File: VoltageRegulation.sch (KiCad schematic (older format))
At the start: 83 parts, among them Q201 TIP41, Q202 TIP41, Q203 TIP42, U201 LM7812_TO220, U202 LM7805_TO220, U203 Step Down Module +15 to 7v - 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, U204 LM7912_TO220, U205 XL6009 Module DCDC 19 to 30v, U206 TL071, U207 LM78M05_TO252, U208 LM78M12_TO252, U209 MC79M12_TO252

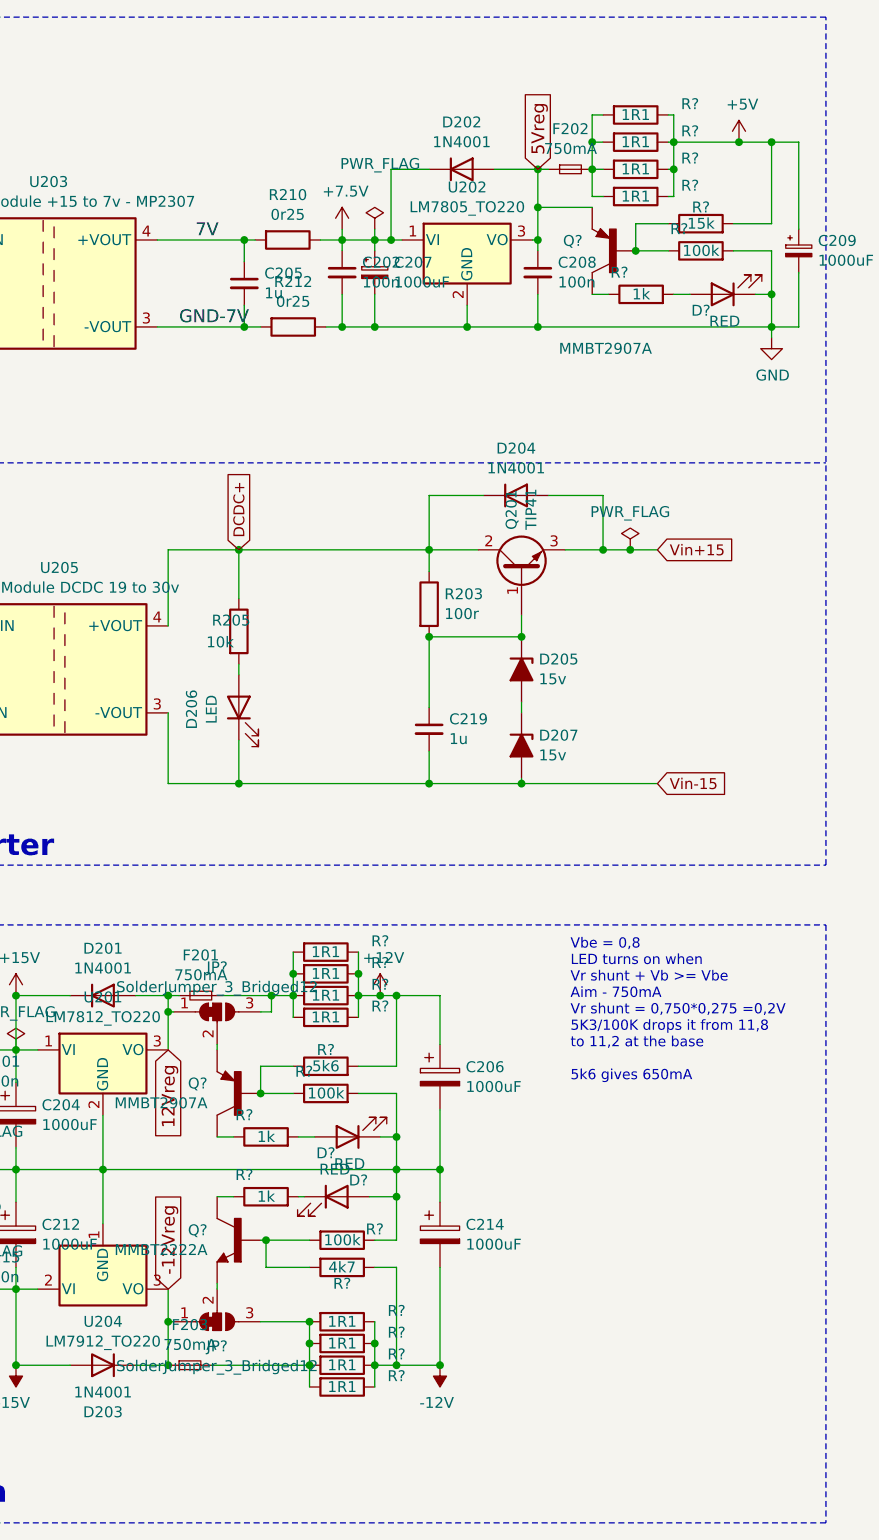
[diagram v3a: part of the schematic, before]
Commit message: placing first components
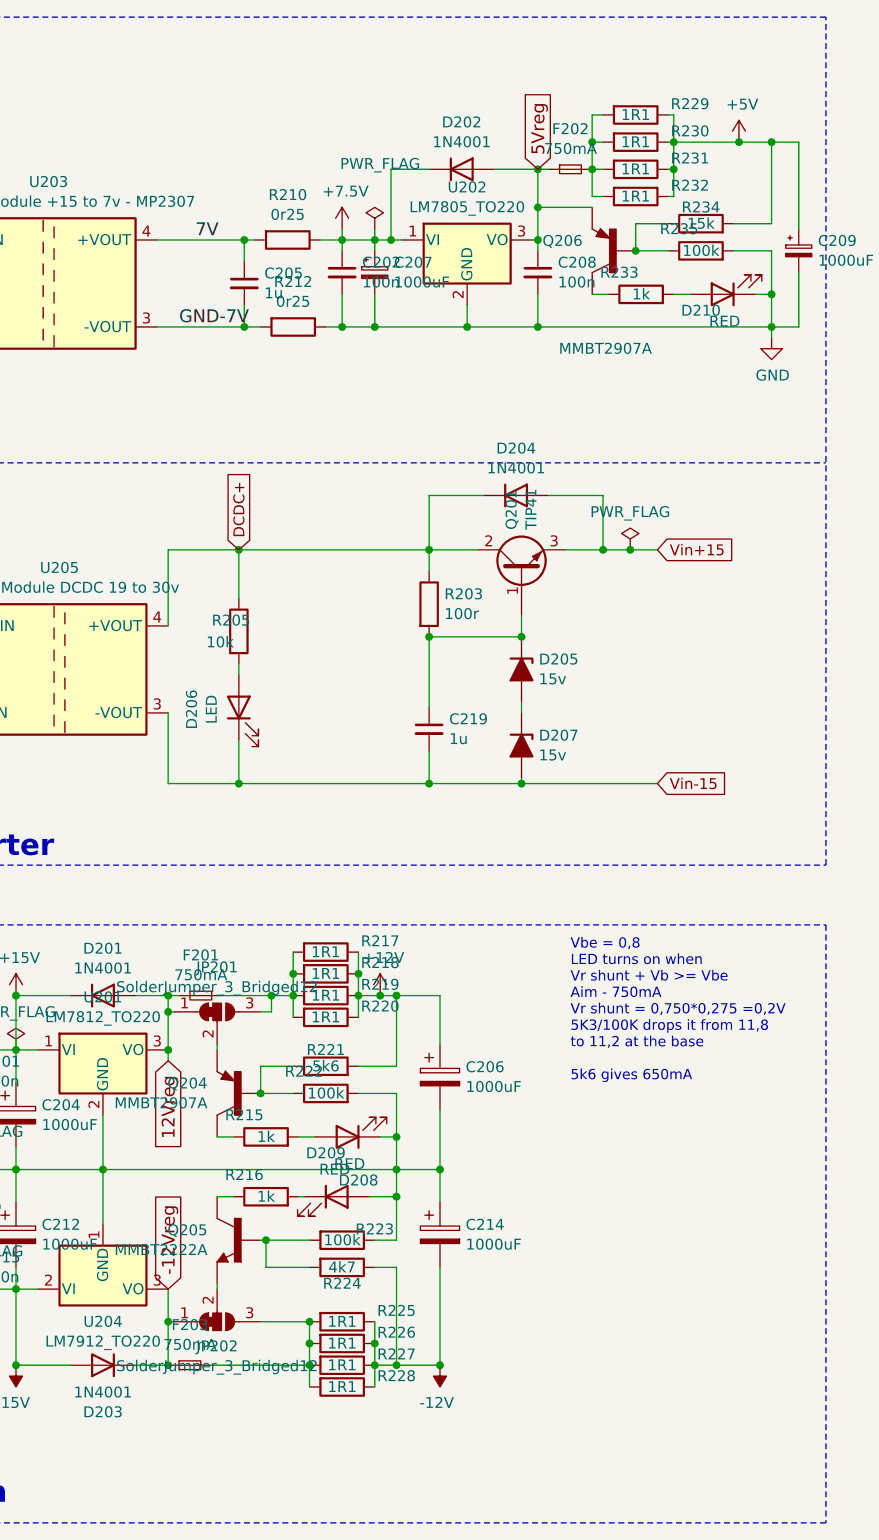
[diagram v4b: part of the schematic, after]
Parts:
- gave numbers to parts that had none: 29
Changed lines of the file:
@@
 Text GLabel 2675 6525 1    59   Input ~ 0
 -12Vreg
-Text GLabel 2675 5425 3    59   Input ~ 0
+Text GLabel 2675 5475 3    59   Input ~ 0
 12Vreg
 $Comp
@@
 U 1 1 5E8B7031
 P 3000 5625
-F 0 "Q?" H 3144 5671 50  0000 L CNN
+AR Path="/5E8B7031" Ref="Q?"  Part="1"
+AR Path="/5CBAA806/5E8B7031" Ref="Q204"  Part="1"
+F 0 "Q204" H 3144 5671 50  0000 L CNN
 F 1 "MMBT2907A" H 3144 5580 50  0000 L CNN
 F 2 "" H 3000 5625 98  0001 C CNN
@@
 U 1 1 5E8B7037
 P 3650 5175
-F 0 "#PWR?" H 3650 5025 50  0001 C CNN
+AR Path="/5E8B7037" Ref="#PWR?"  Part="1"
+AR Path="/5CBAA806/5E8B7037" Ref="#PWR0208"  Part="1"
+F 0 "#PWR0208" H 3650 5025 50  0001 C CNN
 F 1 "+12V" H 3665 5348 50  0000 C CNN
 F 2 "" H 3650 5175 50  0001 C CNN
@@
 U 1 1 5E8B7043
 P 3400 5175
-F 0 "R?" V 3350 5425 50  0000 C CNN
+AR Path="/5E8B7043" Ref="R?"  Part="1"
+AR Path="/5CBAA806/5E8B7043" Ref="R219"  Part="1"
+F 0 "R219" V 3350 5425 50  0000 C CNN
 F 1 "1R1" V 3400 5175 50  0000 C CNN
 F 2 "Resistor_SMD:R_0805_2012Metric_Pad1.15x1.40mm_HandSolder" V 3330 5175 50  0001 C CNN
@@
 U 1 1 5E8B7049
 P 3400 5275
-F 0 "R?" V 3350 5525 50  0000 C CNN
+AR Path="/5E8B7049" Ref="R?"  Part="1"
+AR Path="/5CBAA806/5E8B7049" Ref="R220"  Part="1"
+F 0 "R220" V 3350 5525 50  0000 C CNN
 F 1 "1R1" V 3400 5275 50  0000 C CNN
 F 2 "Resistor_SMD:R_0805_2012Metric_Pad1.15x1.40mm_HandSolder" V 3330 5275 50  0001 C CNN
@@
 U 1 1 5E8B705A
 P 3125 5825
-F 0 "R?" V 3225 5925 50  0000 C CNN
+AR Path="/5E8B705A" Ref="R?"  Part="1"
+AR Path="/5CBAA806/5E8B705A" Ref="R215"  Part="1"
+F 0 "R215" V 3225 5925 50  0000 C CNN
 F 1 "1k" V 3125 5825 50  0000 C CNN
 F 2 "Resistor_SMD:R_0805_2012Metric_Pad1.15x1.40mm_HandSolder" V 3055 5825 50  0001 C CNN
@@
 U 1 1 5E8B7060
 P 3500 5825
-F 0 "D?" H 3600 5900 50  0000 C CNN
+AR Path="/5E8B7060" Ref="D?"  Part="1"
+AR Path="/5CBAA806/5E8B7060" Ref="D209"  Part="1"
+F 0 "D209" H 3600 5900 50  0000 C CNN
 F 1 "RED" H 3491 5950 50  0000 C CNN
 F 2 "LED_THT:LED_D5.0mm" H 3500 5825 50  0001 C CNN
@@
 P 3400 5500
 AR Path="/5E8B706D" Ref="R?"  Part="1"
-AR Path="/5CBAA806/5E8B706D" Ref="R?"  Part="1"
-F 0 "R?" V 3475 5500 50  0000 C CNN
+AR Path="/5CBAA806/5E8B706D" Ref="R221"  Part="1"
+F 0 "R221" V 3475 5500 50  0000 C CNN
 F 1 "5k6" V 3400 5500 50  0000 C CNN
 F 2 "Resistor_SMD:R_0805_2012Metric_Pad1.15x1.40mm_HandSolder" V 3330 5500 50  0001 C CNN
@@
 U 1 1 5E8B7078
 P 3400 5625
-F 0 "R?" V 3500 5725 50  0000 C CNN
+AR Path="/5E8B7078" Ref="R?"  Part="1"
+AR Path="/5CBAA806/5E8B7078" Ref="R222"  Part="1"
+F 0 "R222" V 3500 5725 50  0000 C CNN
 F 1 "100k" V 3400 5625 50  0000 C CNN
 F 2 "Resistor_SMD:R_0805_2012Metric_Pad1.15x1.40mm_HandSolder" V 3330 5625 50  0001 C CNN
@@
 U 1 1 5E8B7088
 P 3400 4975
-F 0 "R?" V 3350 5225 50  0000 C CNN
+AR Path="/5E8B7088" Ref="R?"  Part="1"
+AR Path="/5CBAA806/5E8B7088" Ref="R217"  Part="1"
+F 0 "R217" V 3350 5225 50  0000 C CNN
 F 1 "1R1" V 3400 4975 50  0000 C CNN
 F 2 "Resistor_SMD:R_0805_2012Metric_Pad1.15x1.40mm_HandSolder" V 3330 4975 50  0001 C CNN
@@
 U 1 1 5E8B708E
 P 3400 5075
-F 0 "R?" V 3350 5325 50  0000 C CNN
+AR Path="/5E8B708E" Ref="R?"  Part="1"
+AR Path="/5CBAA806/5E8B708E" Ref="R218"  Part="1"
+F 0 "R218" V 3350 5325 50  0000 C CNN
 F 1 "1R1" V 3400 5075 50  0000 C CNN
 F 2 "Resistor_SMD:R_0805_2012Metric_Pad1.15x1.40mm_HandSolder" V 3330 5075 50  0001 C CNN
@@
 U 1 1 5EB67E20
 P 3125 6100
-F 0 "R?" V 3225 6200 50  0000 C CNN
+AR Path="/5EB67E20" Ref="R?"  Part="1"
+AR Path="/5CBAA806/5EB67E20" Ref="R216"  Part="1"
+F 0 "R216" V 3225 6200 50  0000 C CNN
 F 1 "1k" V 3125 6100 50  0000 C CNN
 F 2 "Resistor_SMD:R_0805_2012Metric_Pad1.15x1.40mm_HandSolder" V 3055 6100 50  0001 C CNN
@@
 U 1 1 5EB67E2A
 P 3450 6100
-F 0 "D?" H 3550 6175 50  0000 C CNN
+AR Path="/5EB67E2A" Ref="D?"  Part="1"
+AR Path="/5CBAA806/5EB67E2A" Ref="D208"  Part="1"
+F 0 "D208" H 3550 6175 50  0000 C CNN
 F 1 "RED" H 3441 6225 50  0000 C CNN
 F 2 "LED_THT:LED_D5.0mm" H 3450 6100 50  0001 C CNN
@@
 	3725 6100 3725 5975
 $Comp
-L MMBT2222A:MMBT2222A Q?
+L MMBT2222A:MMBT2222A Q205
 U 1 1 5EBAABA8
 P 3000 6300
-F 0 "Q?" H 3144 6346 50  0000 L CNN
+F 0 "Q205" H 3144 6346 50  0000 L CNN
 F 1 "MMBT2222A" H 3144 6255 50  0000 L CNN
 F 2 "SOT23" H 3000 6300 50  0001 L BNN
@@
 P 3475 6425
 AR Path="/5EBC9441" Ref="R?"  Part="1"
-AR Path="/5CBAA806/5EBC9441" Ref="R?"  Part="1"
-F 0 "R?" V 3550 6425 50  0000 C CNN
+AR Path="/5CBAA806/5EBC9441" Ref="R224"  Part="1"
+F 0 "R224" V 3550 6425 50  0000 C CNN
 F 1 "4k7" V 3475 6425 50  0000 C CNN
 F 2 "Resistor_SMD:R_0805_2012Metric_Pad1.15x1.40mm_HandSolder" V 3405 6425 50  0001 C CNN
@@
 U 1 1 5EBC944B
 P 3475 6300
-F 0 "R?" V 3425 6450 50  0000 C CNN
+AR Path="/5EBC944B" Ref="R?"  Part="1"
+AR Path="/5CBAA806/5EBC944B" Ref="R223"  Part="1"
+F 0 "R223" V 3425 6450 50  0000 C CNN
 F 1 "100k" V 3475 6300 50  0000 C CNN
 F 2 "Resistor_SMD:R_0805_2012Metric_Pad1.15x1.40mm_HandSolder" V 3405 6300 50  0001 C CNN
@@
 U 1 1 5EF36F65
 P 4825 1375
-F 0 "R?" V 4775 1625 50  0000 C CNN
+AR Path="/5EF36F65" Ref="R?"  Part="1"
+AR Path="/5CBAA806/5EF36F65" Ref="R231"  Part="1"
+F 0 "R231" V 4775 1625 50  0000 C CNN
 F 1 "1R1" V 4825 1375 50  0000 C CNN
 F 2 "Resistor_SMD:R_0805_2012Metric_Pad1.15x1.40mm_HandSolder" V 4755 1375 50  0001 C CNN
@@
 U 1 1 5EF36F6F
 P 4825 1500
-F 0 "R?" V 4775 1750 50  0000 C CNN
+AR Path="/5EF36F6F" Ref="R?"  Part="1"
+AR Path="/5CBAA806/5EF36F6F" Ref="R232"  Part="1"
+F 0 "R232" V 4775 1750 50  0000 C CNN
 F 1 "1R1" V 4825 1500 50  0000 C CNN
 F 2 "Resistor_SMD:R_0805_2012Metric_Pad1.15x1.40mm_HandSolder" V 4755 1500 50  0001 C CNN
@@
 U 1 1 5EF36F81
 P 4825 1125
-F 0 "R?" V 4775 1375 50  0000 C CNN
+AR Path="/5EF36F81" Ref="R?"  Part="1"
+AR Path="/5CBAA806/5EF36F81" Ref="R229"  Part="1"
+F 0 "R229" V 4775 1375 50  0000 C CNN
 F 1 "1R1" V 4825 1125 50  0000 C CNN
 F 2 "Resistor_SMD:R_0805_2012Metric_Pad1.15x1.40mm_HandSolder" V 4755 1125 50  0001 C CNN
@@
 U 1 1 5EF36F8B
 P 4825 1250
-F 0 "R?" V 4775 1500 50  0000 C CNN
+AR Path="/5EF36F8B" Ref="R?"  Part="1"
+AR Path="/5CBAA806/5EF36F8B" Ref="R230"  Part="1"
+F 0 "R230" V 4775 1500 50  0000 C CNN
 F 1 "1R1" V 4825 1250 50  0000 C CNN
 F 2 "Resistor_SMD:R_0805_2012Metric_Pad1.15x1.40mm_HandSolder" V 4755 1250 50  0001 C CNN
@@
 U 1 1 5EEC4ABD
 P 5125 1750
-F 0 "R?" V 5225 1850 50  0000 C CNN
+AR Path="/5EEC4ABD" Ref="R?"  Part="1"
+AR Path="/5CBAA806/5EEC4ABD" Ref="R235"  Part="1"
+F 0 "R235" V 5225 1850 50  0000 C CNN
 F 1 "100k" V 5125 1750 50  0000 C CNN
 F 2 "Resistor_SMD:R_0805_2012Metric_Pad1.15x1.40mm_HandSolder" V 5055 1750 50  0001 C CNN
@@
 P 5125 1625
 AR Path="/5EEC4AB7" Ref="R?"  Part="1"
-AR Path="/5CBAA806/5EEC4AB7" Ref="R?"  Part="1"
-F 0 "R?" V 5200 1625 50  0000 C CNN
+AR Path="/5CBAA806/5EEC4AB7" Ref="R234"  Part="1"
+F 0 "R234" V 5200 1625 50  0000 C CNN
 F 1 "15k" V 5125 1625 50  0000 C CNN
 F 2 "Resistor_SMD:R_0805_2012Metric_Pad1.15x1.40mm_HandSolder" V 5055 1625 50  0001 C CNN
@@
 U 1 1 5EEC4AB1
 P 5225 1950
-F 0 "D?" H 5325 2025 50  0000 C CNN
+AR Path="/5EEC4AB1" Ref="D?"  Part="1"
+AR Path="/5CBAA806/5EEC4AB1" Ref="D210"  Part="1"
+F 0 "D210" H 5325 2025 50  0000 C CNN
 F 1 "RED" H 5216 2075 50  0000 C CNN
 F 2 "LED_THT:LED_D5.0mm" H 5225 1950 50  0001 C CNN
@@
 U 1 1 5EEC4AAB
 P 4850 1950
-F 0 "R?" V 4950 2050 50  0000 C CNN
+AR Path="/5EEC4AAB" Ref="R?"  Part="1"
+AR Path="/5CBAA806/5EEC4AAB" Ref="R233"  Part="1"
+F 0 "R233" V 4950 2050 50  0000 C CNN
 F 1 "1k" V 4850 1950 50  0000 C CNN
 F 2 "Resistor_SMD:R_0805_2012Metric_Pad1.15x1.40mm_HandSolder" V 4780 1950 50  0001 C CNN
@@
 U 1 1 5EEC4AA5
 P 4725 1750
-F 0 "Q?" H 4869 1796 50  0000 L CNN
+AR Path="/5EEC4AA5" Ref="Q?"  Part="1"
+AR Path="/5CBAA806/5EEC4AA5" Ref="Q206"  Part="1"
+F 0 "Q206" H 4869 1796 50  0000 L CNN
 F 1 "MMBT2907A" H 4550 1300 50  0000 L CNN
 F 2 "" H 4725 1750 98  0001 C CNN
@@
 	2375 5975 3725 5975
 $Comp
-L Jumper:SolderJumper_3_Bridged12 JP?
+L Jumper:SolderJumper_3_Bridged12 JP201
 U 1 1 5F0BEA21
 P 2900 5250
-F 0 "JP?" H 2900 5455 50  0000 C CNN
+F 0 "JP201" H 2900 5455 50  0000 C CNN
 F 1 "SolderJumper_3_Bridged12" H 2900 5364 50  0000 C CNN
 F 2 "" H 2900 5250 50  0001 C CNN
@@
 U 1 1 5F233189
 P 3475 6875
-F 0 "R?" V 3425 7125 50  0000 C CNN
+AR Path="/5F233189" Ref="R?"  Part="1"
+AR Path="/5CBAA806/5F233189" Ref="R227"  Part="1"
+F 0 "R227" V 3425 7125 50  0000 C CNN
 F 1 "1R1" V 3475 6875 50  0000 C CNN
 F 2 "Resistor_SMD:R_0805_2012Metric_Pad1.15x1.40mm_HandSolder" V 3405 6875 50  0001 C CNN
@@
 U 1 1 5F233193
 P 3475 6975
-F 0 "R?" V 3425 7225 50  0000 C CNN
+AR Path="/5F233193" Ref="R?"  Part="1"
+AR Path="/5CBAA806/5F233193" Ref="R228"  Part="1"
+F 0 "R228" V 3425 7225 50  0000 C CNN
 F 1 "1R1" V 3475 6975 50  0000 C CNN
 F 2 "Resistor_SMD:R_0805_2012Metric_Pad1.15x1.40mm_HandSolder" V 3405 6975 50  0001 C CNN
@@
 U 1 1 5F23319D
 P 3475 6675
-F 0 "R?" V 3425 6925 50  0000 C CNN
+AR Path="/5F23319D" Ref="R?"  Part="1"
+AR Path="/5CBAA806/5F23319D" Ref="R225"  Part="1"
+F 0 "R225" V 3425 6925 50  0000 C CNN
 F 1 "1R1" V 3475 6675 50  0000 C CNN
 F 2 "Resistor_SMD:R_0805_2012Metric_Pad1.15x1.40mm_HandSolder" V 3405 6675 50  0001 C CNN
@@
 U 1 1 5F2331A7
 P 3475 6775
-F 0 "R?" V 3425 7025 50  0000 C CNN
+AR Path="/5F2331A7" Ref="R?"  Part="1"
+AR Path="/5CBAA806/5F2331A7" Ref="R226"  Part="1"
+F 0 "R226" V 3425 7025 50  0000 C CNN
 F 1 "1R1" V 3475 6775 50  0000 C CNN
 F 2 "Resistor_SMD:R_0805_2012Metric_Pad1.15x1.40mm_HandSolder" V 3405 6775 50  0001 C CNN
@@
 	2875 6875 3325 6875
 $Comp
-L Jumper:SolderJumper_3_Bridged12 JP?
+L Jumper:SolderJumper_3_Bridged12 JP202
 U 1 1 5F2CD980
 P 2900 6675
-F 0 "JP?" H 2900 6788 50  0000 C CNN
+F 0 "JP202" H 2900 6788 50  0000 C CNN
 F 1 "SolderJumper_3_Bridged12" H 2900 6879 50  0000 C CNN
 F 2 "" H 2900 6675 50  0001 C CNN
@@
 Wire Wire Line
 	2675 6675 2675 6875
+Wire Wire Line
+	2675 5475 2675 5425
+Connection ~ 2675 5425
 $EndSCHEMATC

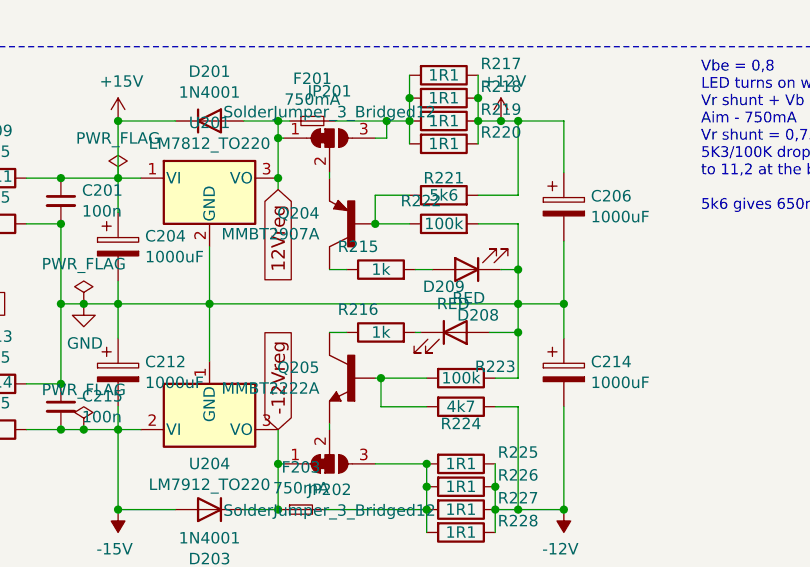
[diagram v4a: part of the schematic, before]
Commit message: Update VoltageRegulation.sch
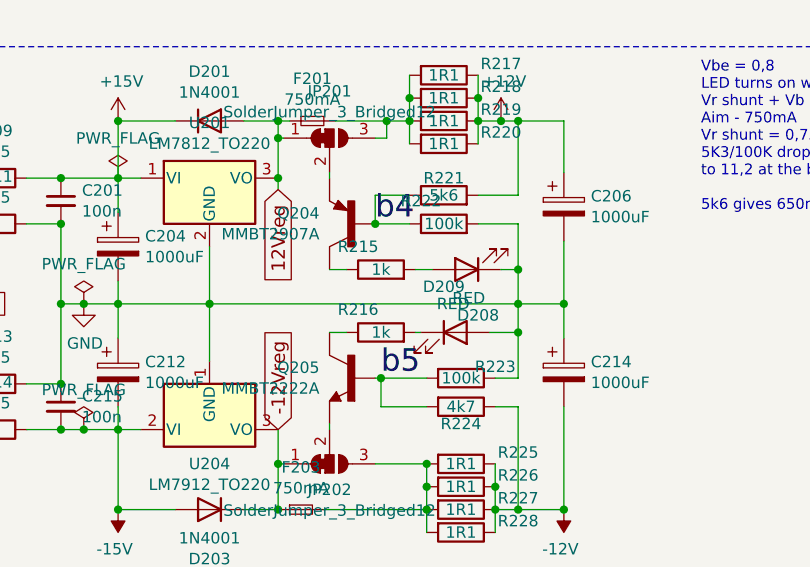
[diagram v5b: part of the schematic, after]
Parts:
- JP201, JP202: footprint (none) -> Jumper:SolderJumper-3_P1.3mm_Bridged12_RoundedPad1.0x1.5mm_NumberLabels
- Q204, Q206: footprint (none) -> Package_TO_SOT_SMD:SOT-23_Handsoldering
- Q205: footprint SOT23 -> Package_TO_SOT_SMD:SOT-23_Handsoldering
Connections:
- net b4: now reaches Q204.B, R221.1, R222.1
- net b5: now reaches Q205.1 (B), R223.2, R224.2
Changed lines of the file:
@@
 F 0 "Q204" H 3144 5671 50  0000 L CNN
 F 1 "MMBT2907A" H 3144 5580 50  0000 L CNN
-F 2 "" H 3000 5625 98  0001 C CNN
+F 2 "Package_TO_SOT_SMD:SOT-23_Handsoldering" H 3000 5625 98  0001 C CNN
 F 3 "SOT-23-3 ON Semiconductor" H 3000 5625 50  0001 L BNN
 F 4 "ON Semiconductor" H 3000 5625 50  0001 L BNN "Field4"
@@
 F 0 "Q205" H 3144 6346 50  0000 L CNN
 F 1 "MMBT2222A" H 3144 6255 50  0000 L CNN
-F 2 "SOT23" H 3000 6300 50  0001 L BNN
+F 2 "Package_TO_SOT_SMD:SOT-23_Handsoldering" H 3000 6300 50  0001 L BNN
 F 3 "Unavailable" H 3000 6300 50  0001 L BNN
 F 4 "None" H 3000 6300 50  0001 L BNN "Field4"
@@
 F 0 "Q206" H 4869 1796 50  0000 L CNN
 F 1 "MMBT2907A" H 4550 1300 50  0000 L CNN
-F 2 "" H 4725 1750 98  0001 C CNN
+F 2 "Package_TO_SOT_SMD:SOT-23_Handsoldering" H 4725 1750 98  0001 C CNN
 F 3 "SOT-23-3 ON Semiconductor" H 4725 1750 50  0001 L BNN
 F 4 "ON Semiconductor" H 4725 1750 50  0001 L BNN "Field4"
@@
 F 0 "JP201" H 2900 5455 50  0000 C CNN
 F 1 "SolderJumper_3_Bridged12" H 2900 5364 50  0000 C CNN
-F 2 "" H 2900 5250 50  0001 C CNN
+F 2 "Jumper:SolderJumper-3_P1.3mm_Bridged12_RoundedPad1.0x1.5mm_NumberLabels" H 2900 5250 50  0001 C CNN
 F 3 "~" H 2900 5250 50  0001 C CNN
 	1    2900 5250
@@
 F 0 "JP202" H 2900 6788 50  0000 C CNN
 F 1 "SolderJumper_3_Bridged12" H 2900 6879 50  0000 C CNN
-F 2 "" H 2900 6675 50  0001 C CNN
+F 2 "Jumper:SolderJumper-3_P1.3mm_Bridged12_RoundedPad1.0x1.5mm_NumberLabels" H 2900 6675 50  0001 C CNN
 F 3 "~" H 2900 6675 50  0001 C CNN
 	1    2900 6675
@@
 	2675 5475 2675 5425
 Connection ~ 2675 5425
+Text Label 3100 5625 0    98   ~ 0
+b4
+Text Label 3125 6300 0    98   ~ 0
+b5
 $EndSCHEMATC

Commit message: interboard connector
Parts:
- Q204, Q206: symbol MMBT2907A:MMBT2907A -> MMBT2907_:MMBT2907*
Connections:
- net labels added: I+12, I+5, I-12
- wire segments 248 -> 254
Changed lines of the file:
@@
 $EndComp
 $Comp
-L MMBT2907A:MMBT2907A Q?
+L MMBT2907_:MMBT2907* Q?
 U 1 1 5E8B7031
 P 3000 5625
@@
 $EndComp
 $Comp
-L MMBT2907A:MMBT2907A Q?
+L MMBT2907_:MMBT2907* Q?
 U 1 1 5EEC4AA5
 P 4725 1750
@@
 Text Label 3125 6300 0    98   ~ 0
 b5
+Text GLabel 2875 6050 0    59   Input ~ 0
+I-12
+Wire Wire Line
+	2900 6100 2900 6050
+Wire Wire Line
+	2900 6050 2875 6050
+Connection ~ 2900 6100
+Text GLabel 2875 5900 0    59   Input ~ 0
+I+12
+Wire Wire Line
+	2875 5900 2900 5900
+Wire Wire Line
+	2900 5900 2900 5825
+Connection ~ 2900 5825
+Text GLabel 4600 2025 0    59   Input ~ 0
+I+5
+Wire Wire Line
+	4600 2025 4625 2025
+Wire Wire Line
+	4625 2025 4625 1950
+Connection ~ 4625 1950
 $EndSCHEMATC

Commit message: Real life pictures
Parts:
- Q204, Q206: symbol MMBT2907_:MMBT2907* -> KicadJE-EuroPowerSupply2-rescue:MMBT2907*-MMBT2907_
- Q205: symbol MMBT2222A:MMBT2222A -> KicadJE-EuroPowerSupply2-rescue:MMBT2222A-MMBT2222A
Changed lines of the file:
@@
 $EndComp
 $Comp
-L MMBT2907_:MMBT2907* Q?
+L KicadJE-EuroPowerSupply2-rescue:MMBT2907*-MMBT2907_ Q?
 U 1 1 5E8B7031
 P 3000 5625
@@
 	3725 6100 3725 5975
 $Comp
-L MMBT2222A:MMBT2222A Q205
+L KicadJE-EuroPowerSupply2-rescue:MMBT2222A-MMBT2222A Q205
 U 1 1 5EBAABA8
 P 3000 6300
+AR Path="/5EBAABA8" Ref="Q205"  Part="1"
+AR Path="/5CBAA806/5EBAABA8" Ref="Q205"  Part="1"
 F 0 "Q205" H 3144 6346 50  0000 L CNN
 F 1 "MMBT2222A" H 3144 6255 50  0000 L CNN
@@
 $EndComp
 $Comp
-L MMBT2907_:MMBT2907* Q?
+L KicadJE-EuroPowerSupply2-rescue:MMBT2907*-MMBT2907_ Q?
 U 1 1 5EEC4AA5
 P 4725 1750
